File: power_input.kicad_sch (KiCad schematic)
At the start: 95 parts, among them J201 61300211121, J202 61300211121, J203 61300211121, J204 61300211121, J205 61300211121, J206 61300211121, J207 61300211121, J208 61300211121, Q201 DMPH4029LFGQ, Q202 DMPH4029LFGQ, Q203 IRFL4315PbF, Q204 DMPH4029LFGQ, Q205 DMPH4029LFGQ, U201 LM4040-5.0, U202 TL331, U203 OPA197, U204 LM4040-5.0, U205 TL331, U206 LM4040-5.0, U207 TL331

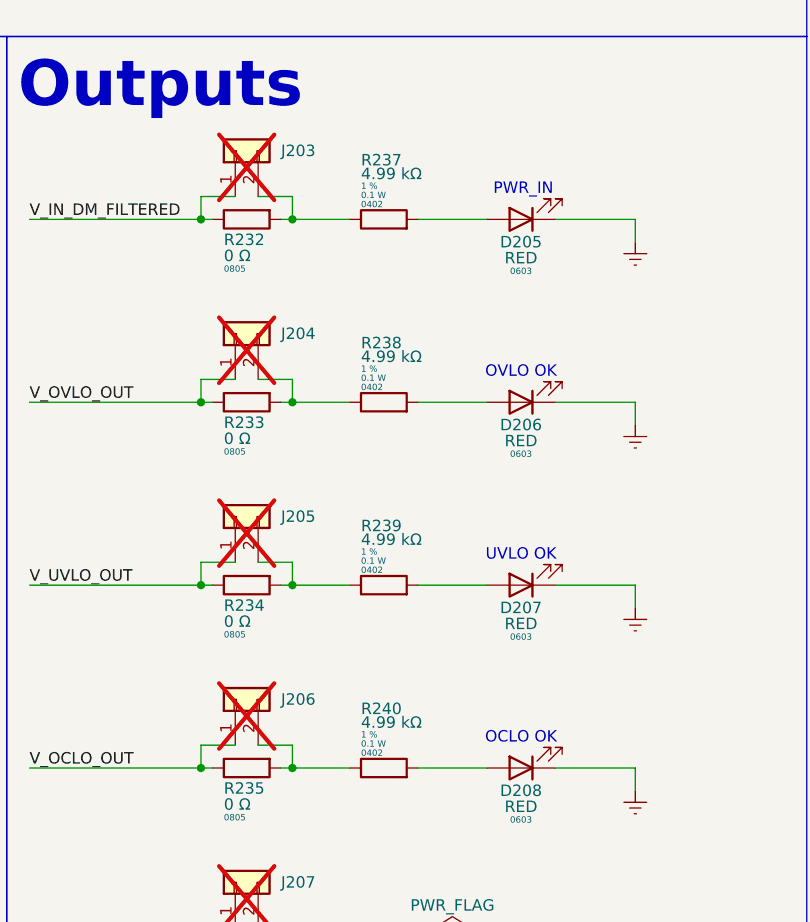
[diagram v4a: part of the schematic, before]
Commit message: Decrease LED brightness
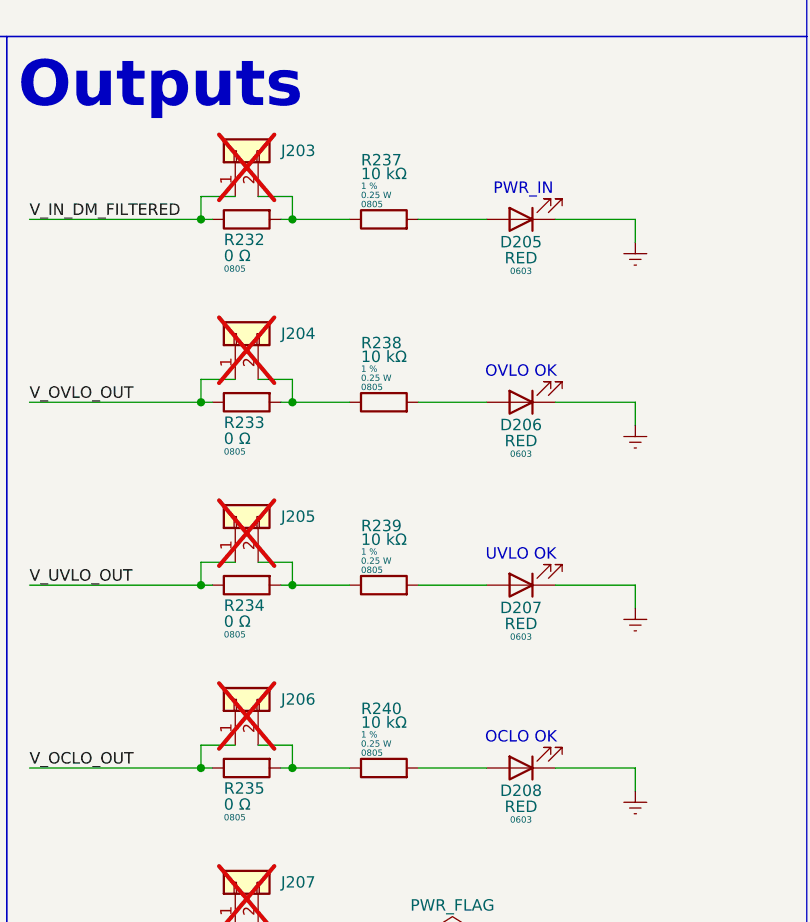
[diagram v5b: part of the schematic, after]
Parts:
- R237, R238, R239, R240: value 4.99 kΩ -> 10 kΩ; footprint perfect_footprints:R_0402_1005Metric_HDI -> Resistor_SMD:R_0805_2012Metric; Digi-Key Part Number 732-560112110247CT-ND -> 541-10.0KCCT-ND; MPN 560112110247 -> CRCW080510K0FKEA; Manufacturer Würth Elektronik -> Vishay Dale; Power rating 0.1 W -> 0.25 W; Size 0402 -> 0805

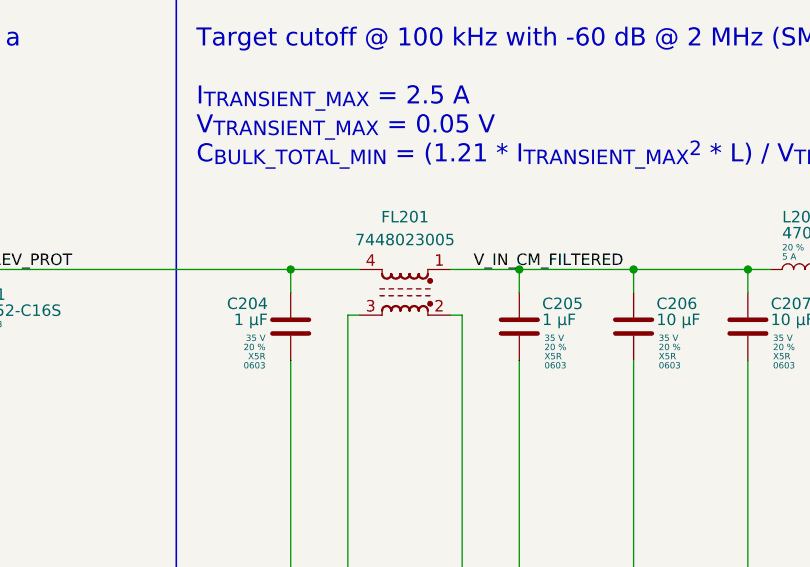
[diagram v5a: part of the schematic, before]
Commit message: Fix common mode choke symbol
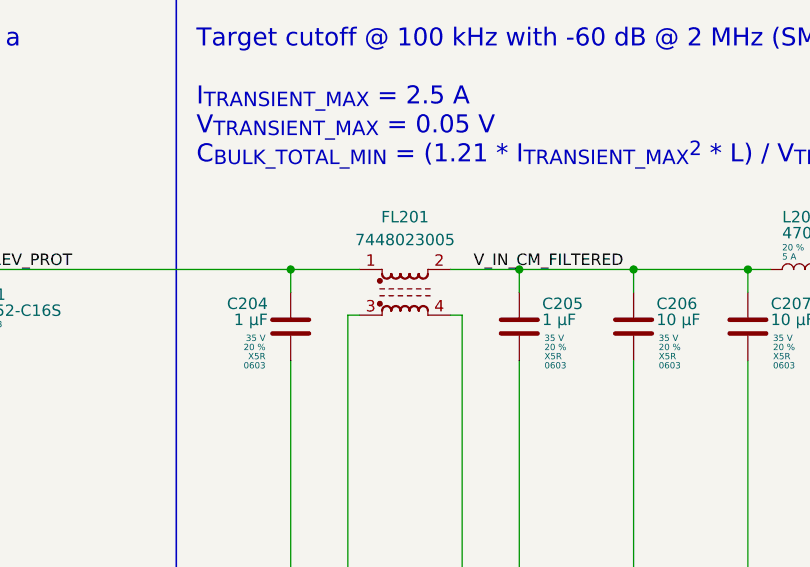
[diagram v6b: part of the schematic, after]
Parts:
- FL201: symbol Filter:Choke_CommonMode_FerriteCore_1423 -> Filter:Choke_CommonMode_FerriteCore_1234
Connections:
- net GND: now also FL201.4; no longer FL201.2
- net V_IN_CM_FILTERED: now also FL201.2; no longer FL201.1
- net V_IN_REV_PROT: now also FL201.1; no longer FL201.4
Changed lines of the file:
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@@
 	)
 	(symbol
-		(lib_id "Filter:Choke_CommonMode_FerriteCore_1423")
+		(lib_id "Filter:Choke_CommonMode_FerriteCore_1234")
 		(at 127 78.74 0)
-		(mirror y)
 		(unit 1)
 		(exclude_from_sim no)

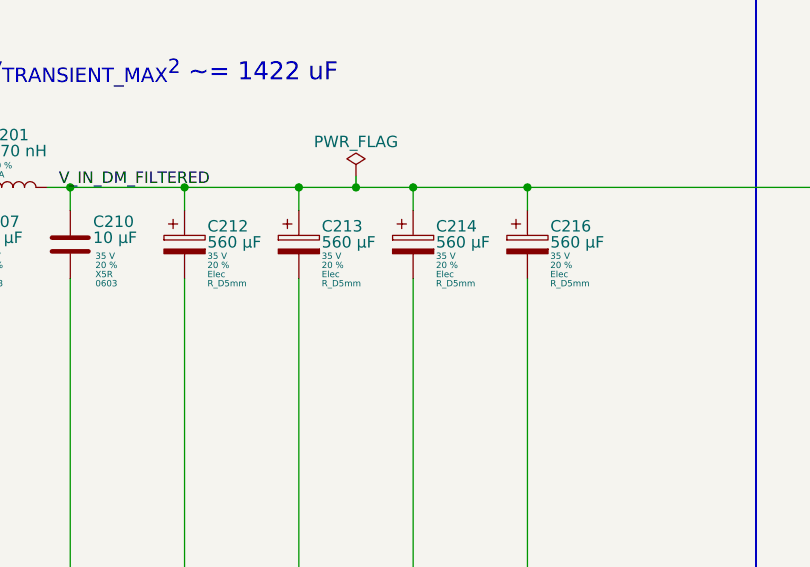
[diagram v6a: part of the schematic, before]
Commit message: Fix EMI filter bulk cap footprints
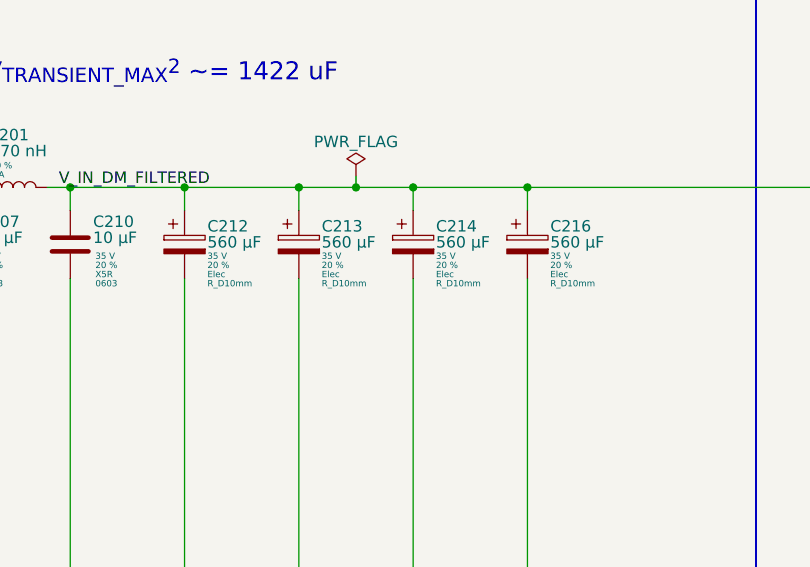
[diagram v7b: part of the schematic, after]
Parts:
- C212, C213, C214, C216: footprint Capacitor_THT:CP_Radial_D5.0mm_P2.00mm -> Capacitor_THT:CP_Radial_D10.0mm_P5.00mm; Size R_D5mm -> R_D10mm

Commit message: Refactor passives
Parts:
- removed C201, C220: 4.7 µF, Capacitor_SMD:C_0603_1608Metric, symbol Device:C
- removed C208: 3300 pF, perfect_footprints:C_0201_0603Metric, symbol Device:C
- removed C211, C218, C223: 0.1 µF, perfect_footprints:C_0201_0603Metric, symbol Device:C
- added C207: 3300 pF, perfect_footprints:C_0402_1005Metric_HDI, symbol Device:C
- added C219: 1 µF, Capacitor_SMD:C_0603_1608Metric, symbol Device:C
- C202: value 0.1 µF -> 1 µF; footprint perfect_footprints:C_0201_0603Metric -> Capacitor_SMD:C_0603_1608Metric; Digi-Key Part Number 490-10430-1-ND -> 490-12330-1-ND; MPN GRM033R6YA104KE14D -> GRT188R61H105KE13D; Size 0201 -> 0603; Tolerance 10 % -> 20 %
- C209, C215: value 4.7 µF -> 1 µF; Digi-Key Part Number 490-7205-1-ND -> 490-12330-1-ND; MPN GRM188R6YA475KE15D -> GRT188R61H105KE13D
- renumbered C203 to C201, C204 to C203, C205 to C204, C206 to C205, C207 to C206, C210 to C208, C212 to C210, C213 to C211, C214 to C212, C216 to C213, C217 to C214, C219 to C216, C221 to C217, C222 to C218
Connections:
- net GND: now also C219.2
- net OCLO_IN_N: now also C207.2
- net OCLO_IN_P: now also C207.1
- net V_IN_DM_FILTERED: now also C219.1
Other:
- moved on the sheet: R230
